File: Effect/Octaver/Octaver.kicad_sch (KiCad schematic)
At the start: 29 parts, among them J1 Conn_01x04_Pin, Q1 DMMT5551, Q2 DMMT5551

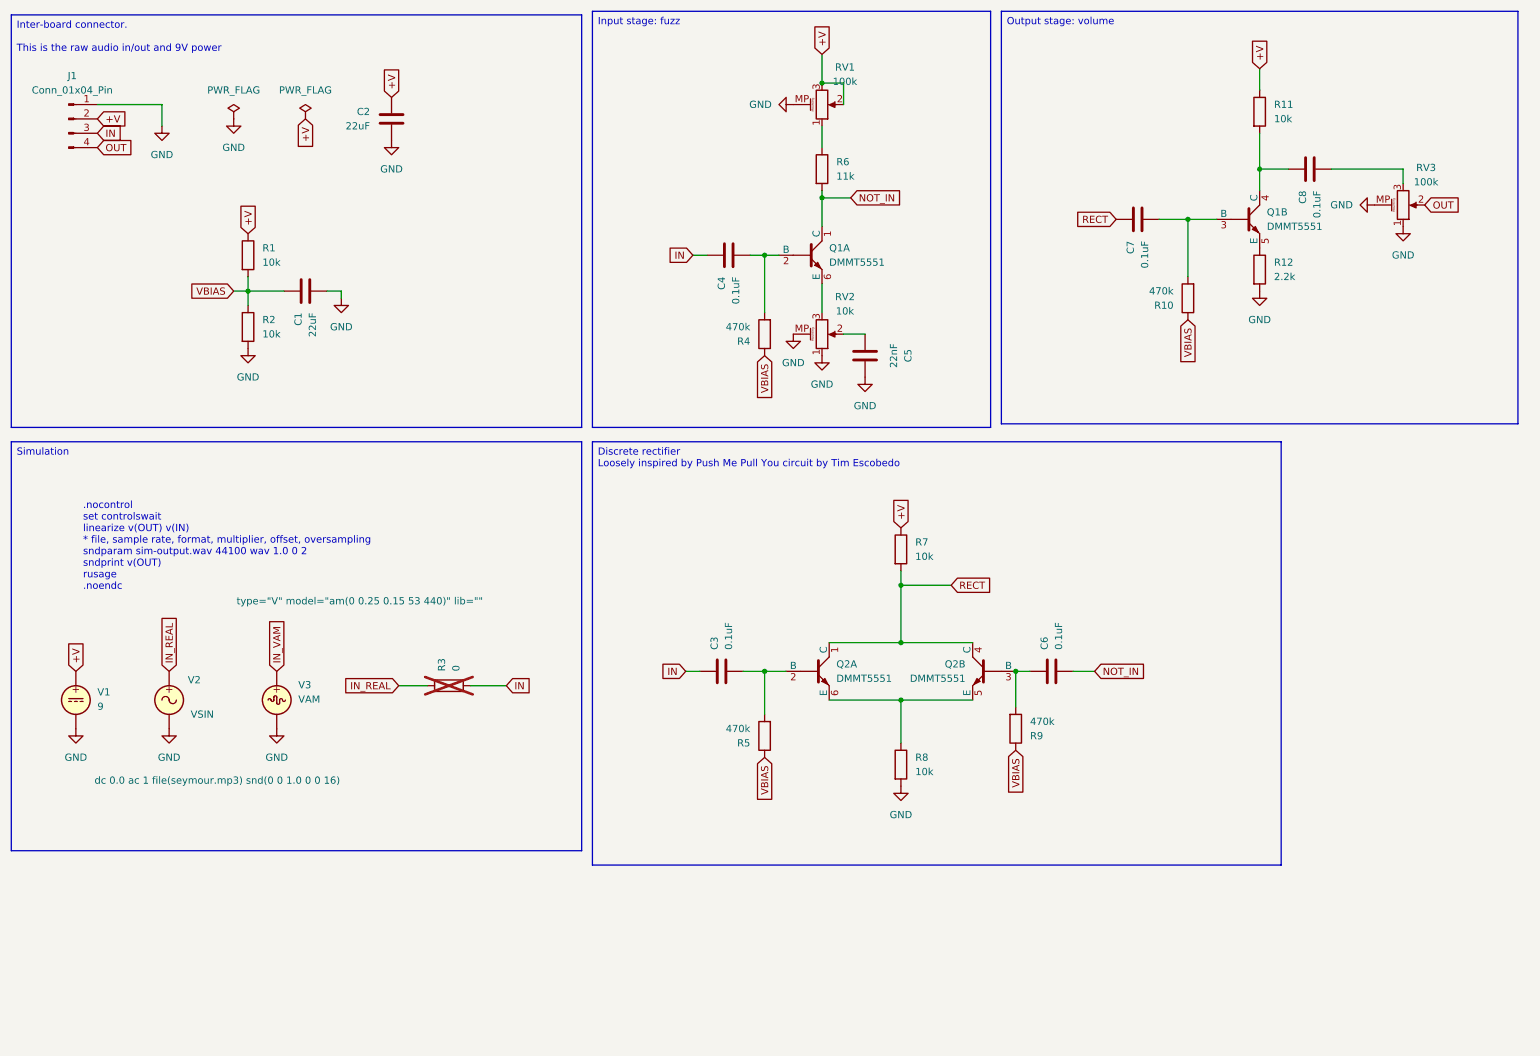
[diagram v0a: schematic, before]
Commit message: First revisions from gen3 testing...
It turns out that while the single connector was sufficient, it is also
mechanically annoyingly less robust than the two separate pin headers we
used to have.

So even though we don't need the extra pins, just split it up into
"power" and a "signal" connectors again.  The placement behind the
output jack was good, so just put the power jack behind the input one
instead.

That ends up making routing nicer with the power trace going down where
it needs to be for the LED anyway, so it's a win-win.  Much nicer than
the old board.  And with the extra pins and the position right next to
the LED, lets just make the base board LED voltage available as an
"active" signal in case anybody ever wants it.

Also, just move the DC blocking capacitor and the anti-pop resistor to
ground to the base board.  Any effects board needs to do that, so it's
one less thing to worry about.  Also add back the low pass RF filter.

With the connector change, this obviously makes the new boards
incompatible, but it's not like I have any legacy boards except for the
test-boards.

On the effect board side, this does the layout changes, but also fixes
the Octaver board that was half-arsed and hadn't done proper bias
voltage calculations.  This basically just reuses them from the boost
board.

Plus use a JFET input on for the Octaver, and while at it make it also
just split the phase the natural way.  Both simpler and more balanced.

So maybe the Octaver works now.

And by "works", I obviously don't mean "sounds good".

Signed-off-by: Linus Torvalds <torvalds@linux-foundation.org>
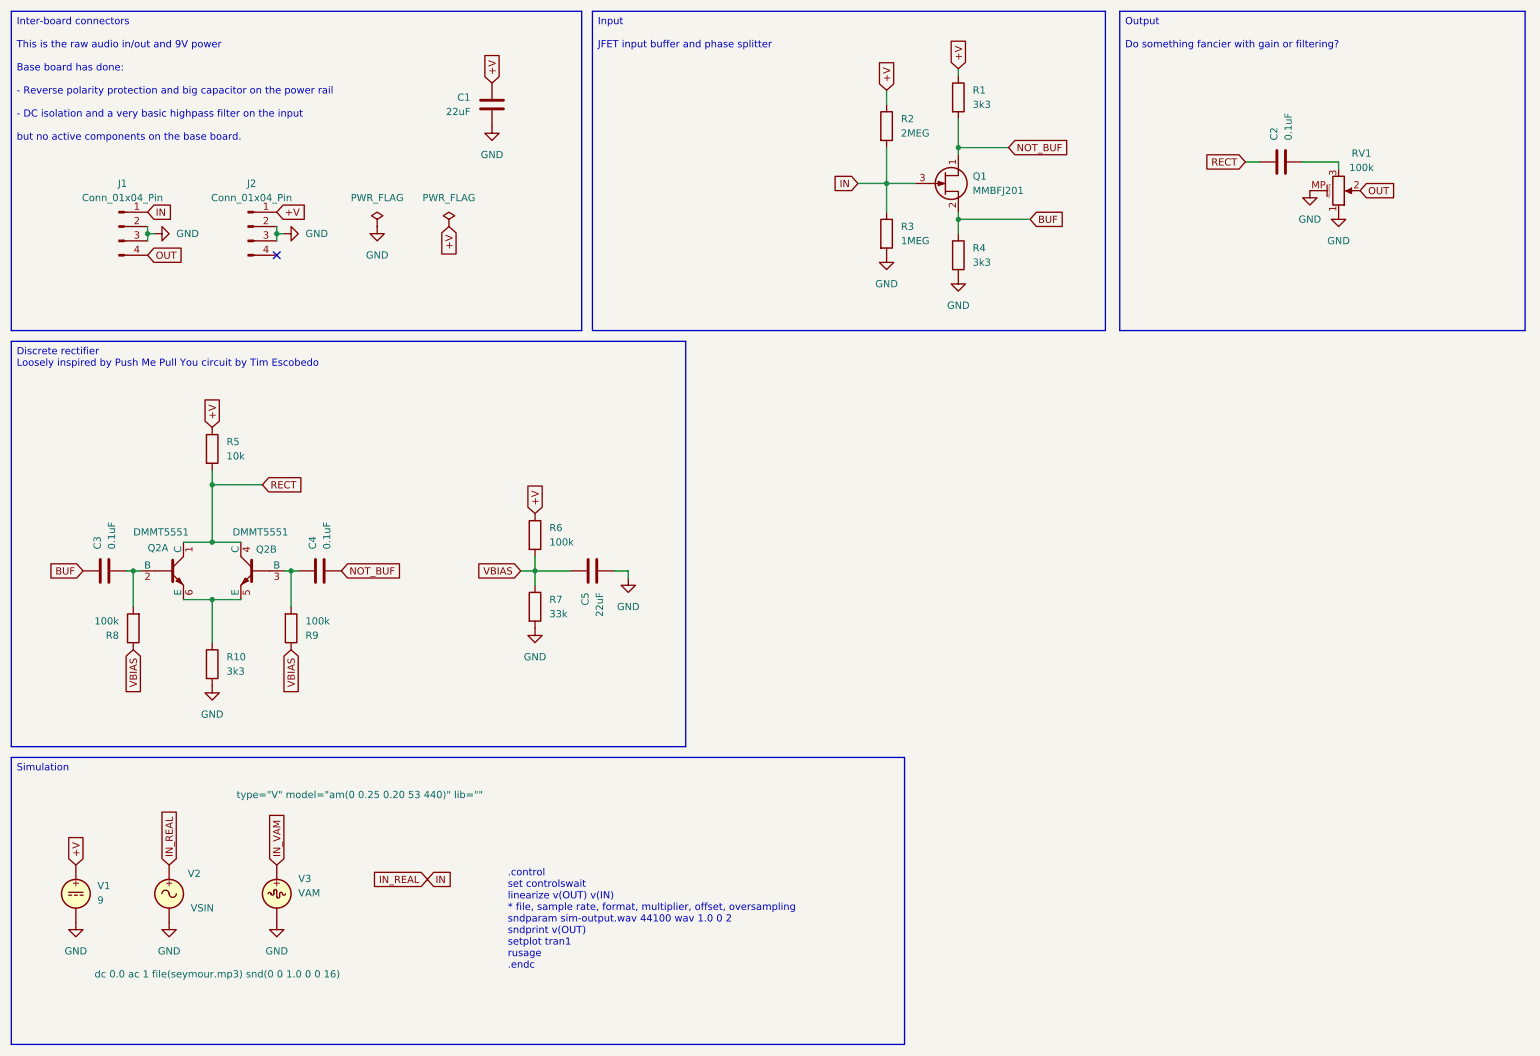
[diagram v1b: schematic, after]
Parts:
- removed C4, C7, C8: 0.1uF, Mylib:C_0704_1810Metric, symbol Device:C
- removed C5: 22nF, Capacitor_SMD:C_0805_2012Metric, symbol Device:C
- removed Q1: DMMT5551, Package_TO_SOT_SMD:SOT-23-6, symbol Mylib:DMMT5551
- removed R10: 470k, Resistor_SMD:R_0805_2012Metric, symbol Device:R
- removed R11: 10k, Resistor_SMD:R_0805_2012Metric, symbol Device:R
- removed R12: 2.2k, Resistor_SMD:R_0805_2012Metric, symbol Device:R
- removed R6: 11k, Resistor_SMD:R_0805_2012Metric, symbol Device:R
- removed RV1: 100k, Mylib:Potentiometer_9mm_MP, symbol Device:R_Potentiometer_MountingPin
- removed RV2: 10k, Mylib:Potentiometer_9mm_MP, symbol Device:R_Potentiometer_MountingPin
- added C2: 0.1uF, Mylib:C_0704_1810Metric, symbol Device:C
- added J2: Conn_01x04_Pin, Connector_PinHeader_2.54mm:PinHeader_1x04_P2.54mm_Vertical, symbol Connector:Conn_01x04_Pin
- added Q1: MMBFJ201, Package_TO_SOT_SMD:SOT-23, symbol Transistor_FET:MMBFJ112
- added R1: 3k3, Resistor_SMD:R_0805_2012Metric, symbol Device:R
- added R2: 2MEG, Resistor_SMD:R_0805_2012Metric, symbol Device:R
- R10: renamed from R8; value 10k -> 3k3
- R3: value 0 -> 1MEG; now fitted; now in the parts list
- R4: value 470k -> 3k3
- R6: renamed from R1; value 10k -> 100k
- R7: renamed from R2; value 10k -> 33k
- R8: renamed from R5; value 470k -> 100k
- R9: value 470k -> 100k
- renumbered C2 to C1, C6 to C4, C1 to C5, R7 to R5, RV3 to RV1
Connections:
- net IN_REAL is gone; now on net IN: R3.1, V2.1
- net +V: now also J2.1 (Pin_1), R1.1, R2.1; no longer J1.2 (Pin_2)
- net GND: now also J1.2 (Pin_2), J1.3 (Pin_3), R3.2, R4.2, J2.2 (Pin_2), J2.3 (Pin_3); no longer J1.1 (Pin_1)
- net IN: now also J1.1 (Pin_1), Q1.3 (G), R2.2; no longer C3.1, J1.3 (Pin_3), R3.2
- net RECT: now also C2.1
- net VBIAS: no longer R4.1
- net at RV1.3: now also C2.2
- net NOT_IN renamed NOT_BUF
- net NOT_BUF: now also Q1.1 (D), R1.2
- new net BUF: C3.1, Q1.2 (S), R4.1
- no-connect marks 0 -> 1
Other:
- note added: ".control set controlswait linearize v(OUT) v(IN) * file, sample rate, format, multiplier, offset, oversampling sndparam sim-output.wav 44100 wav 1.0 0 2 sndprint v(OUT) setplot tran1 rusage .endc"
- note removed: ".nocontrol set controlswait linearize v(OUT) v(IN) * file, sample rate, format, multiplier, offset, oversampling sndparam sim-output.wav 44100 wav 1.0 0 2 sndprint v(OUT) rusage .noendc"
- moved on the sheet: C1, C3, C4, C5, Q2A, Q2B, R10, R5, R6, R7, R8, R9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

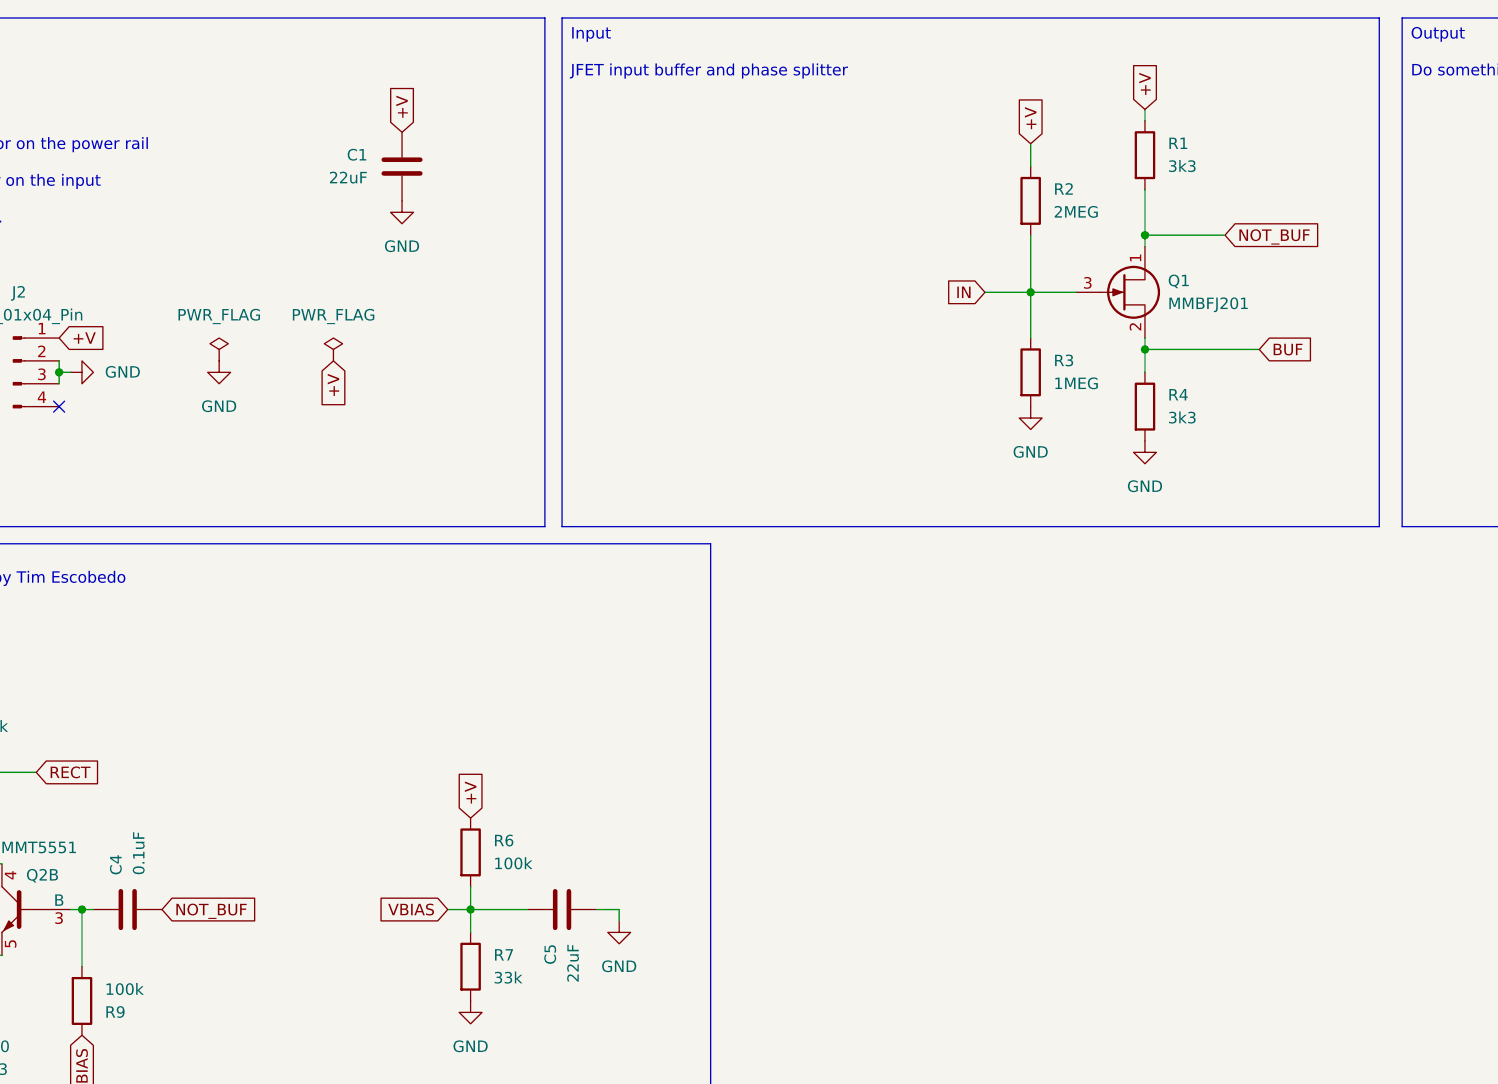
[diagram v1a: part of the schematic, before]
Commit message: Update the Octaver circuit for MMBF5103 use
This not just switching the J201 into a MMBF5103, because when I did
that to verify that it's just a drop-in replacement, the simulation got
very unhappy indeed instead of saying "yup, same thing".

It looks like the extra current going through the 5103 ends up then
going through the subsequent BJT rectification stage, and the two stages
interact in bad ways causing oscillation on the phase-shifted signal.

That is easy enough to fix with just resistors between the stages.  But
I am also unhappy with the simulation voltages because the simulation
isn't seeing the capacitor on the base board, so I'll handle that
separately.

Signed-off-by: Linus Torvalds <torvalds@linux-foundation.org>
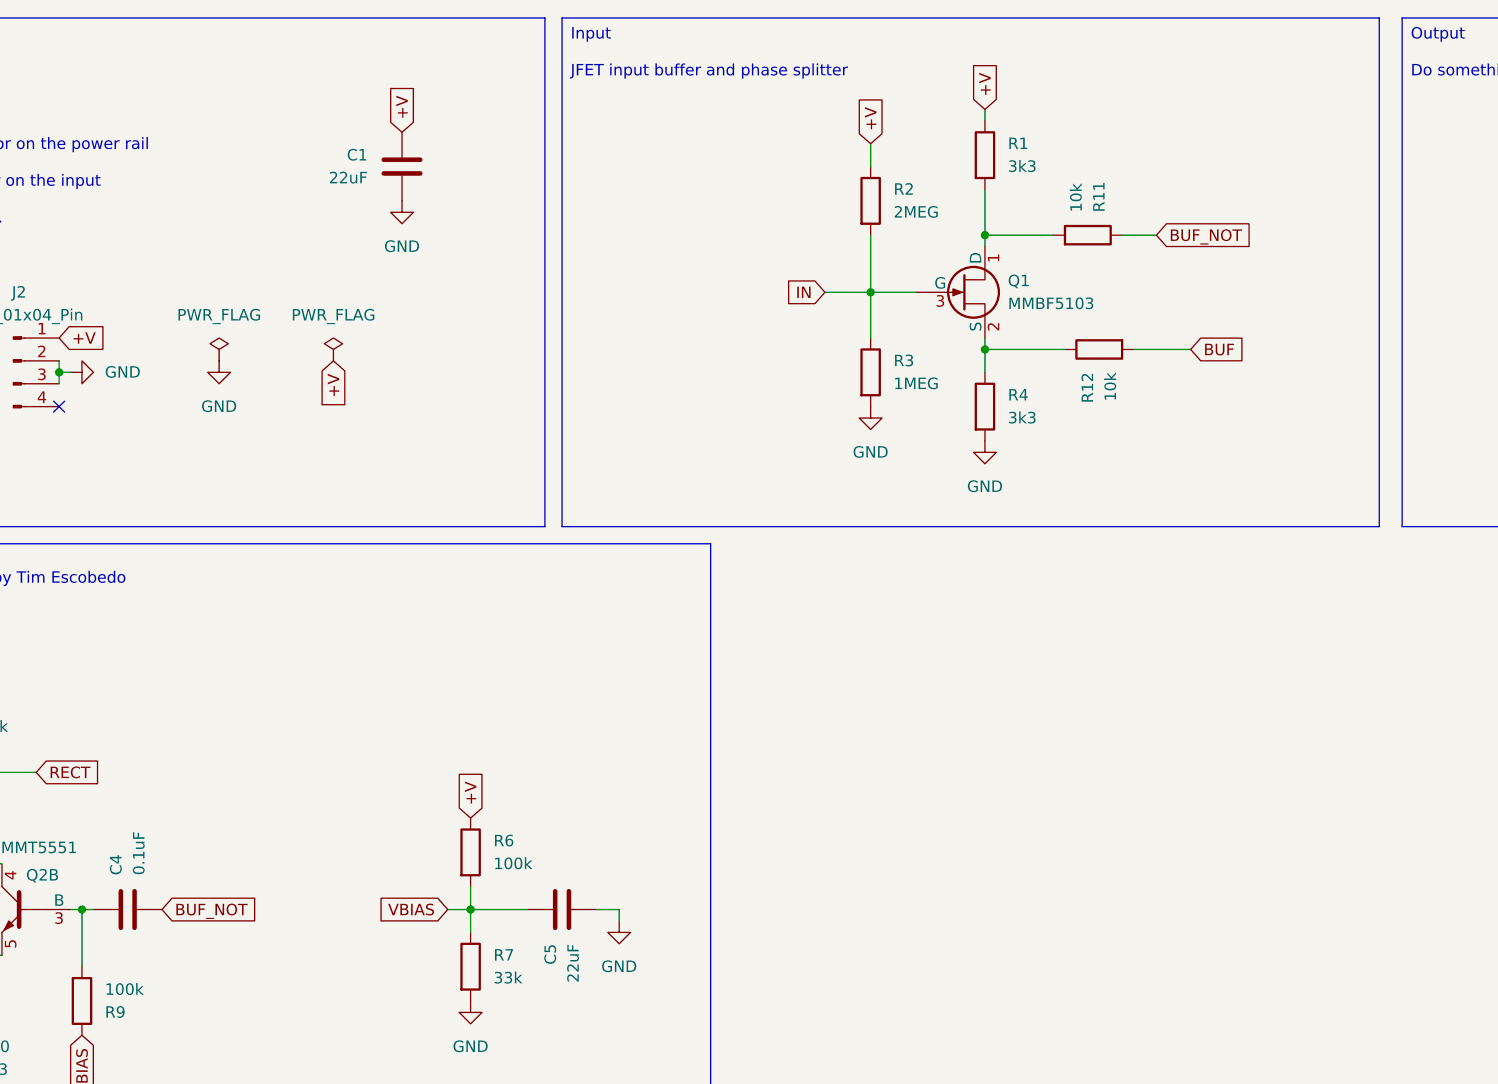
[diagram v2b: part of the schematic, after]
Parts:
- removed Q1: MMBFJ201, Package_TO_SOT_SMD:SOT-23, symbol Transistor_FET:MMBFJ112
- added Q1: MMBF5103, Package_TO_SOT_SMD:SOT-23, symbol Mylib:MMBF5103
- added R11, R12: 10k, Resistor_SMD:R_0805_2012Metric, symbol Device:R
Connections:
- net BUF: now also R12.2; no longer R4.1
- net IN: now also Q1.3 (G)
- net NOT_BUF: no longer names the net of R1.2
- net NOT_BUF: now also Q1.1 (D), R11.2; no longer C4.2
- new net: Q1.2 (S), R12.1, R4.1
- new net BUF_NOT: C4.2, R11.1
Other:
- moved on the sheet: R1, R2, R3, R4
